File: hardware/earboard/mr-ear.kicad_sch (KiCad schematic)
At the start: 25 parts, among them J1 EAR, J2 Conn_01x02, J3 LEFT, J4 RIGHT, U1 TLC5947DAP

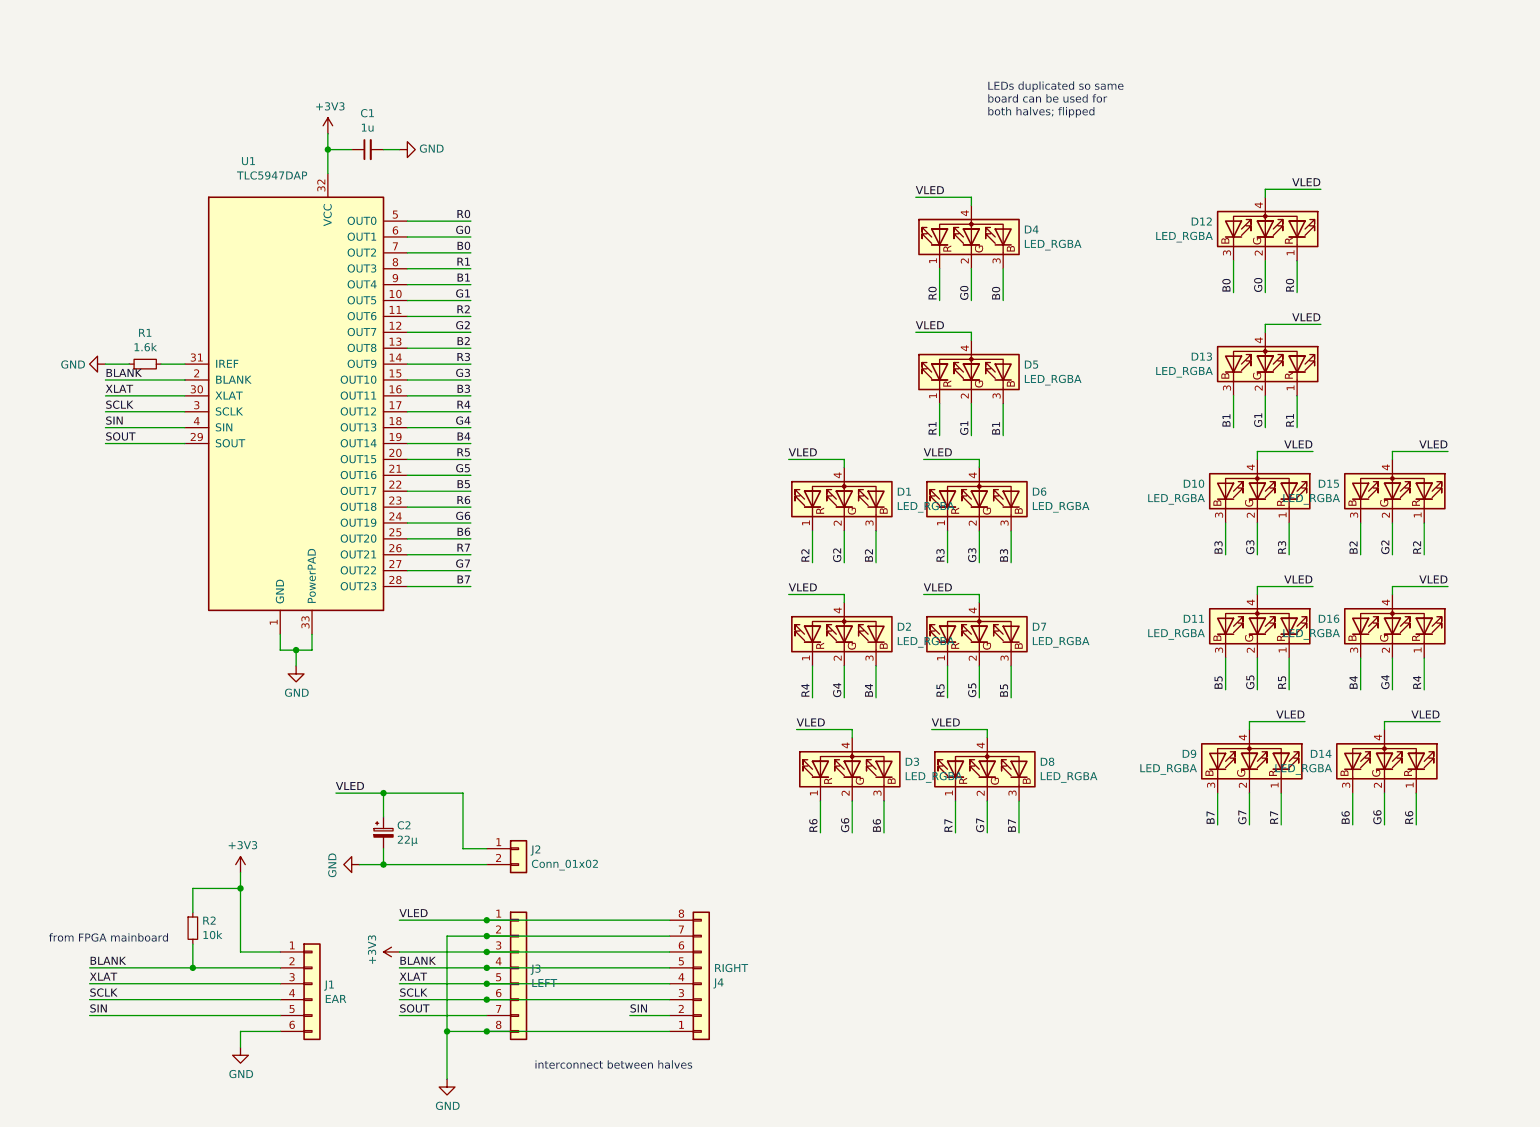
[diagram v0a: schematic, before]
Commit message: Update ear board with addressable LEDs
Signed-off-by: gatecat <gatecat@ds0.me>
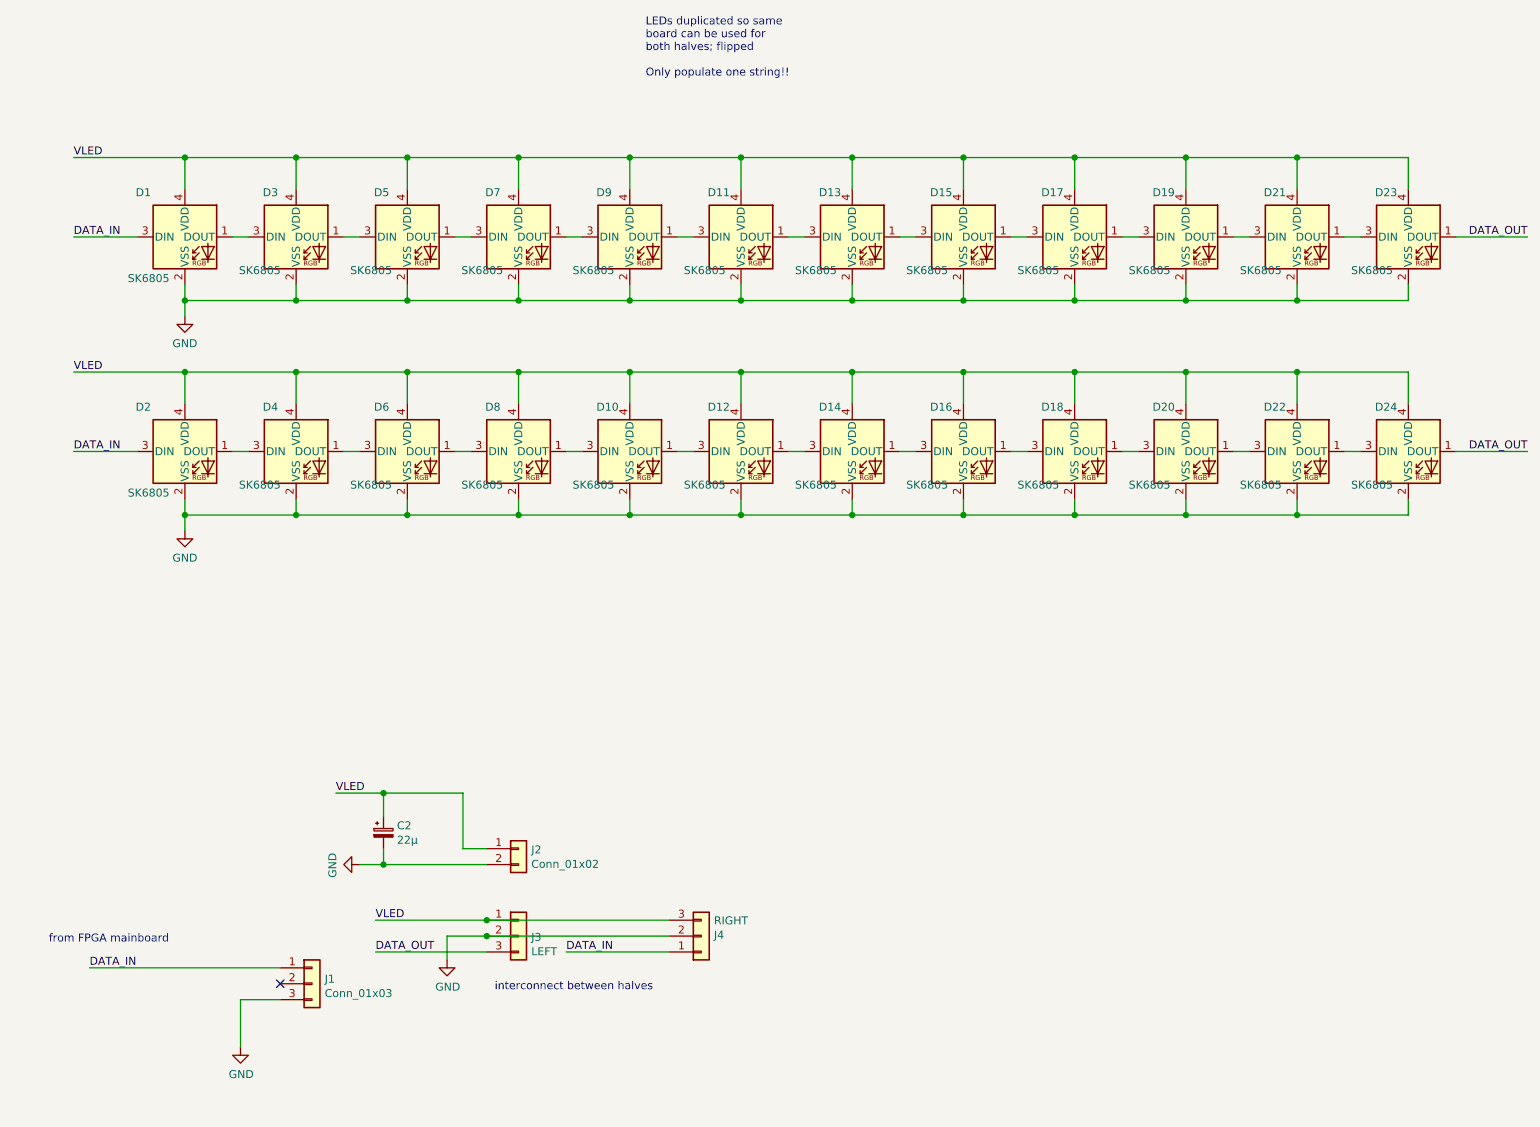
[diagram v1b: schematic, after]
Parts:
- removed C1: 1u, Capacitor_SMD:C_0805_2012Metric, symbol Device:C_Small
- removed D1, D10, D11, D12, D13, D14, D15, D16, D2, D3, D4, D5, D6, D7, D8, D9: LED_RGBA, symbol Device:LED_RGBA
- removed J1: EAR, Connector_PinHeader_2.00mm:PinHeader_1x06_P2.00mm_Vertical_SMD_Pin1Left, symbol Connector_Generic:Conn_01x06
- removed R1: 1.6k, Resistor_SMD:R_0603_1608Metric, symbol Device:R_Small
- removed R2: 10k, Resistor_SMD:R_0603_1608Metric, symbol Device:R_Small
- removed U1: TLC5947DAP, Package_SO:HTSSOP-32-1EP_6.1x11mm_P0.65mm_EP5.2x11mm_Mask4.11x4.36mm_ThermalVias, symbol Driver_LED:TLC5947DAP
- added D1, D10, D11, D12, D13, D14, D15, D16, D17, D18, D19, D2, D20, D21, D22, D23, D24, D3, D4, D5, D6, D7, D8, D9: SK6805, LED_SMD:LED_SK6805_PLCC4_2.4x2.7mm_P1.3mm, symbol LED:SK6805
- added J1: Conn_01x03, Connector_JST:JST_PH_S3B-PH-K_1x03_P2.00mm_Horizontal, symbol Connector_Generic:Conn_01x03
- J3, J4: footprint Connector_PinSocket_2.00mm:PinSocket_1x08_P2.00mm_Vertical_SMD_Pin1Left -> Connector_PinSocket_2.00mm:PinSocket_1x03_P2.00mm_Vertical_SMD_Pin1Left; symbol Connector_Generic:Conn_01x08 -> Connector_Generic:Conn_01x03
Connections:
- net SIN is gone; now on net GND: J4.2 (Pin_2)
- net GND: now also D1.2 (VSS), D10.2 (VSS), D11.2 (VSS), D12.2 (VSS), D13.2 (VSS), D14.2 (VSS), D15.2 (VSS), D16.2 (VSS), D17.2 (VSS), D18.2 (VSS), D19.2 (VSS), D2.2 (VSS), D20.2 (VSS), D21.2 (VSS), D22.2 (VSS), D23.2 (VSS), D24.2 (VSS), D3.2 (VSS), D4.2 (VSS), D5.2 (VSS), D6.2 (VSS), D7.2 (VSS), D8.2 (VSS), D9.2 (VSS), J1.3 (Pin_3); no longer J3.8 (Pin_8), J4.1 (Pin_1), J4.7 (Pin_7)
- net VLED: now also J4.3 (Pin_3), D1.4 (VDD), D10.4 (VDD), D11.4 (VDD), D12.4 (VDD), D13.4 (VDD), D14.4 (VDD), D15.4 (VDD), D16.4 (VDD), D17.4 (VDD), D18.4 (VDD), D19.4 (VDD), D2.4 (VDD), D20.4 (VDD), D21.4 (VDD), D22.4 (VDD), D23.4 (VDD), D24.4 (VDD), D3.4 (VDD), D4.4 (VDD), D5.4 (VDD), D6.4 (VDD), D7.4 (VDD), D8.4 (VDD), D9.4 (VDD); no longer J4.8 (Pin_8)
- net +3V3 renamed DATA_OUT
- net DATA_OUT: now also D23.1 (DOUT), D24.1 (DOUT); no longer J4.6 (Pin_6)
- removed net BLANK: J3.4 (Pin_4), J4.5 (Pin_5)
- removed net SCLK: J3.6 (Pin_6), J4.3 (Pin_3)
- removed net SOUT: J3.7 (Pin_7)
- removed net XLAT: J3.5 (Pin_5), J4.4 (Pin_4)
- new net: D12.1 (DOUT), D14.3 (DIN)
- new net: D10.1 (DOUT), D12.3 (DIN)
- new net: D18.1 (DOUT), D20.3 (DIN)
- new net: D16.1 (DOUT), D18.3 (DIN)
- new net: D2.1 (DOUT), D4.3 (DIN)
- new net: D1.1 (DOUT), D3.3 (DIN)
- new net: D19.1 (DOUT), D21.3 (DIN)
- new net: D17.1 (DOUT), D19.3 (DIN)
- new net: D22.1 (DOUT), D24.3 (DIN)
- new net: D21.1 (DOUT), D23.3 (DIN)
- new net: D5.1 (DOUT), D7.3 (DIN)
- new net: D3.1 (DOUT), D5.3 (DIN)
- new net: D10.3 (DIN), D8.1 (DOUT)
- new net: D6.1 (DOUT), D8.3 (DIN)
- new net: D15.1 (DOUT), D17.3 (DIN)
- new net: D4.1 (DOUT), D6.3 (DIN)
- new net: D11.3 (DIN), D9.1 (DOUT)
- new net: D7.1 (DOUT), D9.3 (DIN)
- new net: D20.1 (DOUT), D22.3 (DIN)
- new net: D11.1 (DOUT), D13.3 (DIN)
- new net: D13.1 (DOUT), D15.3 (DIN)
- new net: D14.1 (DOUT), D16.3 (DIN)
- new net DATA_IN: D1.3 (DIN), D2.3 (DIN), J1.1 (Pin_1), J4.1 (Pin_1)
- no-connect marks 0 -> 1
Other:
- note added: "LEDs duplicated so same board can be used for both halves; flipped Only populate one string!!"
- note removed: "LEDs duplicated so same board can be used for both halves; flipped"
